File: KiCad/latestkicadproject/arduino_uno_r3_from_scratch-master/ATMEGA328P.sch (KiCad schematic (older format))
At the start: 12 parts, among them SW1 RESET_SWITCH, U5 ATMEGA328P, X2 CSTCE16MOV53-R0

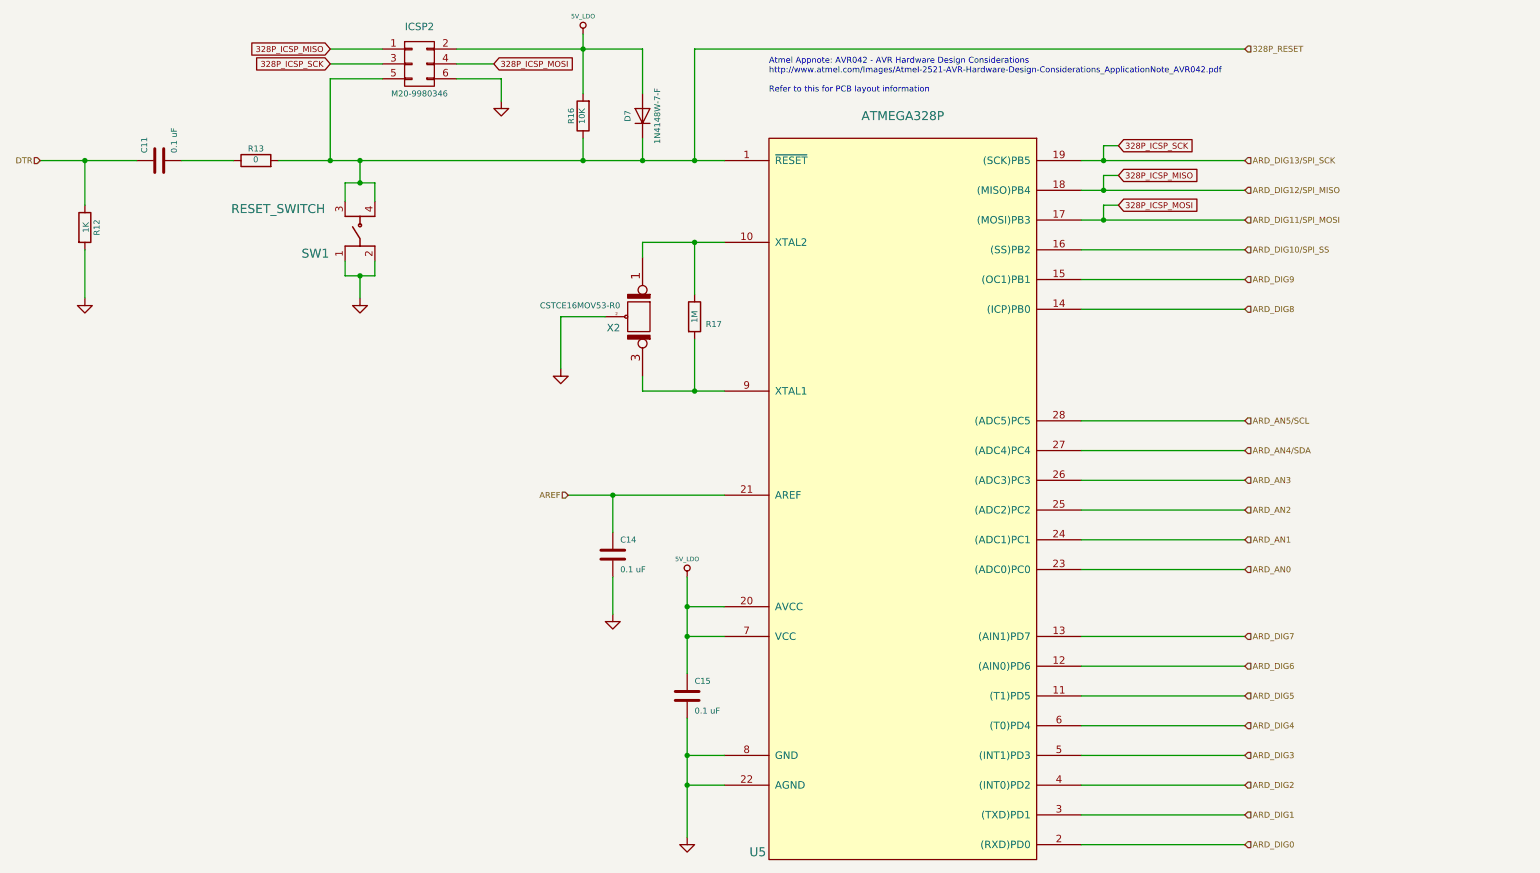
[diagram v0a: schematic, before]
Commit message: 28feb
Aanpassing KiCad+deel footprints
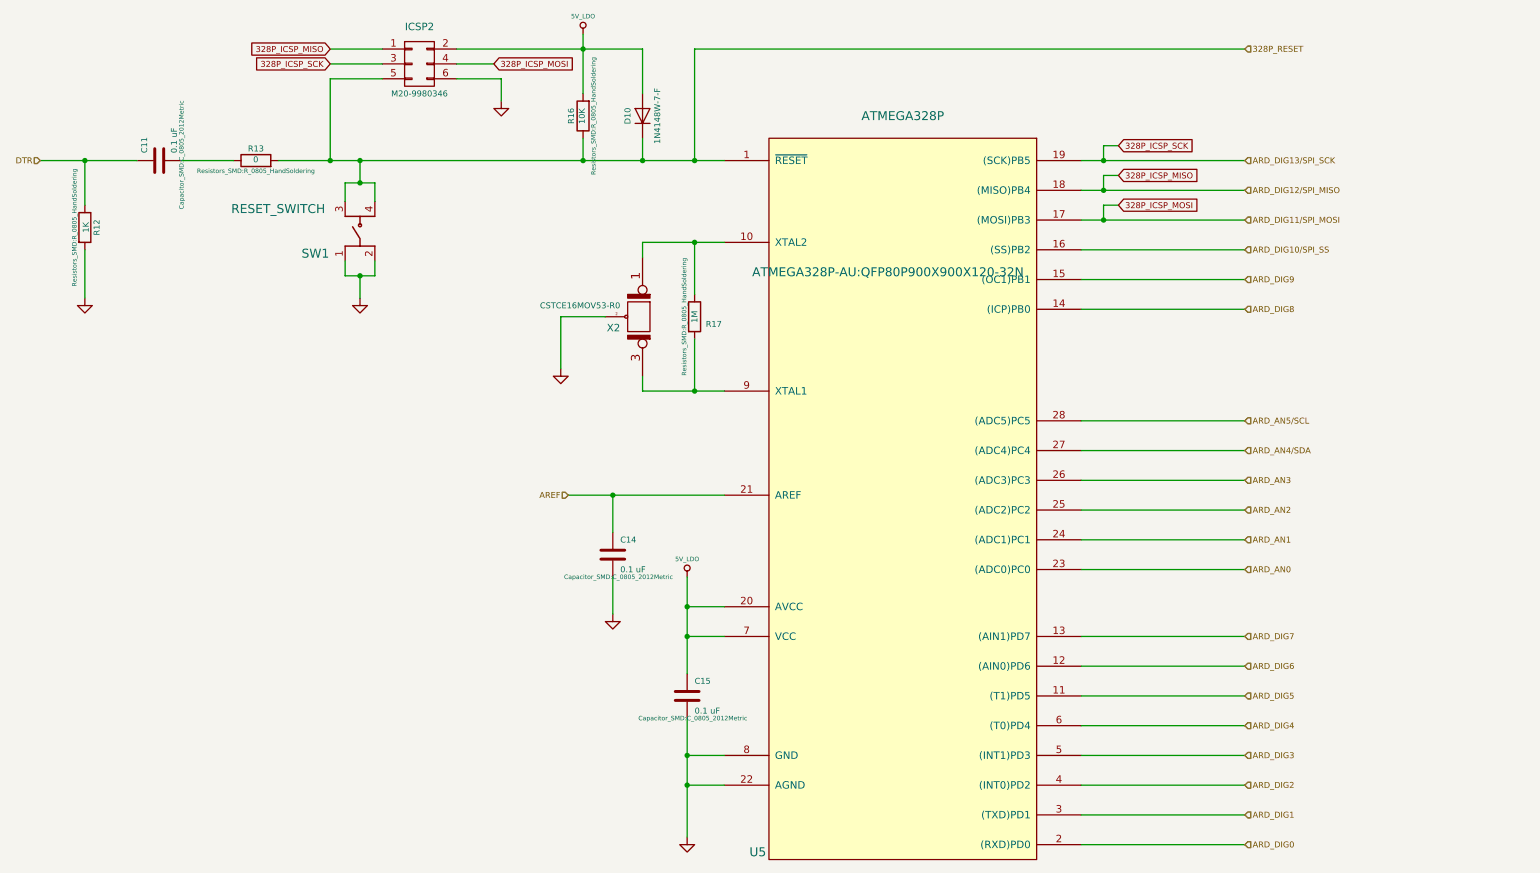
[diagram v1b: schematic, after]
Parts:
- C11, C14, C15: footprint ~ -> Capacitor_SMD:C_0805_2012Metric
- D10: renamed from D7; footprint ~ -> (none)
- ICSP2, X2: footprint ~ -> (none)
- R12, R13, R16, R17: footprint ~ -> Resistors_SMD:R_0805_HandSoldering
- U5: footprint ~ -> ATMEGA328P-AU:QFP80P900X900X120-32N
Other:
- note removed: "Atmel Appnote: AVR042 - AVR Hardware Design Considerations\nhttp://www.atmel.com/Images/Atmel-2521-AVR-Hardware-Design-Considerations_ApplicationNote_AVR042.pdf\n\nRefer to this for PCB layout information"
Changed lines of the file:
@@
 $Descr A4 11693 8268
 encoding utf-8
-Sheet 5 7
+Sheet 7 7
 Title "Arduino UNO R3 Clone"
 Date "8 oct 2015"
@@
 F 0 "U5" H 6075 1350 60  0000 C CNN
 F 1 "ATMEGA328P" H 7050 6300 60  0000 C CNN
-F 2 "~" H 6950 5250 60  0000 C CNN
+F 2 "ATMEGA328P-AU:QFP80P900X900X120-32N" H 6950 5250 60  0000 C CNN
 F 3 "http://www.atmel.com/images/Atmel-8271-8-bit-AVR-Microcontroller-ATmega48A-48PA-88A-88PA-168A-168PA-328-328P_datasheet_Complete.pdf" H 6950 5250 60  0001 C CNN
 F 4 "IC MCU 8BIT 32KB FLASH 28DIP" H 7050 3750 60  0001 C CNN "Characteristics"
@@
 	4800 3750 5850 3750
 $Comp
-L GND-RESCUE-Arduino_Uno_R3_From_Scratch #PWR020
+L GND-RESCUE-Arduino_Uno_R3_From_Scratch #PWR033
 U 1 1 55E8AA8C
 P 5600 6050
-F 0 "#PWR020" H 5600 6050 30  0001 C CNN
+F 0 "#PWR033" H 5600 6050 30  0001 C CNN
 F 1 "GND" H 5600 5980 30  0001 C CNN
 F 2 "~" H 5600 6050 60  0000 C CNN
@@
 F 0 "R12" V 1630 1950 40  0000 C CNN
 F 1 "1K" V 1557 1951 40  0000 C CNN
-F 2 "~" V 1480 1950 30  0000 C CNN
+F 2 "Resistors_SMD:R_0805_HandSoldering" V 1480 1950 30  0000 C CNN
 F 3 "http://images.ihscontent.net/vipimages/VipMasterIC/IC/VISH/VISHS75859/VISHS75859-1.pdf" H 1550 1950 30  0001 C CNN
 F 4 "METAL GLAZE/THICK FILM, 0.125W, 5%, 200ppm, 1000ohm, SURFACE MOUNT, 0805," H 1550 1950 60  0001 C CNN "Characteristics"
@@
 F 0 "ICSP2" H 3800 1100 50  0000 C CNN
 F 1 "M20-9980346" H 3800 650 40  0000 C CNN
-F 2 "~" H 3800 850 60  0000 C CNN
+F 2 "" H 3800 850 60  0000 C CNN
 F 3 "http://cdn.harwin.com/pdfs/M20-998.pdf" H 3800 850 60  0001 C CNN
 F 4 "6 CONTACT(S), MALE, STRAIGHT TWO PART BOARD CONNECTOR" H 3800 850 60  0001 C CNN "Characteristics"
@@
 $EndComp
 $Comp
-L D D7
+L D D10
 U 1 1 55E8CABC
 P 5300 1200
-F 0 "D7" H 5300 1300 40  0000 C CNN
+F 0 "D10" H 5300 1300 40  0000 C CNN
 F 1 "1N4148W-7-F" H 5300 1100 40  0000 C CNN
-F 2 "~" H 5300 1200 60  0000 C CNN
+F 2 "" H 5300 1200 60  0000 C CNN
 F 3 "http://www.diodes.com/_files/datasheets/ds30086.pdf" H 5300 1200 60  0001 C CNN
 F 4 "DIODE GEN PURP 100V 300MA SOD123" H 5300 1200 60  0001 C CNN "Characteristics"
@@
 F 0 "SW1" V 3250 2275 60  0000 C CNN
 F 1 "RESET_SWITCH" V 3550 2525 60  0000 C CNN
-F 2 "" H 3400 1975 60  0000 C CNN
+F 2 "" H 3400 1975 60  0001 C CNN
 F 3 "http://industrial.panasonic.com/www-data/pdf/ATK0000/ATK0000CE28.pdf" H 3400 1975 60  0001 C CNN
 F 4 "SWITCH TACTILE SPST-NO 0.02A 15V" H 3400 1975 60  0001 C CNN "Characteristics"
@@
 	3200 950  3200 1500
 $Comp
-L 5V_LDO #PWR021
+L 5V_LDO #PWR034
 U 1 1 55E95BB4
 P 4900 650
-F 0 "#PWR021" H 4900 740 20  0001 C CNN
+F 0 "#PWR034" H 4900 740 20  0001 C CNN
 F 1 "5V_LDO" H 4900 770 30  0000 C CNN
 F 2 "~" H 4900 650 60  0000 C CNN
@@
 $EndComp
 $Comp
-L 5V_LDO #PWR022
+L 5V_LDO #PWR035
 U 1 1 55E95BC3
 P 5600 4300
-F 0 "#PWR022" H 5600 4390 20  0001 C CNN
+F 0 "#PWR035" H 5600 4390 20  0001 C CNN
 F 1 "5V_LDO" H 5600 4420 30  0000 C CNN
 F 2 "~" H 5600 4300 60  0000 C CNN
@@
 F 0 "R13" V 2780 1500 40  0000 C CNN
 F 1 "0" V 2707 1501 40  0000 C CNN
-F 2 "~" V 2630 1500 30  0000 C CNN
+F 2 "Resistors_SMD:R_0805_HandSoldering" V 2630 1500 30  0000 C CNN
 F 3 "http://industrial.panasonic.com/www-cgi/jvcr13pz.cgi?E+PZ+3+AOA0001+ERJ6GEY0R00V+7+WW" H 2700 1500 30  0001 C CNN
 F 4 "RES SMD 0.0 OHM JUMPER 1/8W 0805" H 2700 1500 60  0001 C CNN "Characteristics"
@@
 F 0 "X2" V 5325 2450 50  0000 R CNN
 F 1 "CSTCE16MOV53-R0" V 5175 2450 40  0000 R CNN
-F 2 "~" H 5250 2550 60  0000 C CNN
+F 2 "" H 5250 2550 60  0000 C CNN
 F 3 "http://www.murata.com/~/media/webrenewal/support/library/catalog/products/timingdevice/ceralock/p16e.ashx" H 5250 2550 60  0001 C CNN
 F 4 "CER RESONATOR 16.0MHZ SMD" H 5250 2550 60  0001 C CNN "Characteristics"
@@
 Wire Wire Line
 	4750 2550 4750 2900
-Text Notes 6150 1050 0    40   ~ 0
-Atmel Appnote: AVR042 - AVR Hardware Design Considerations\nhttp://www.atmel.com/Images/Atmel-2521-AVR-Hardware-Design-Considerations_ApplicationNote_AVR042.pdf\n\nRefer to this for PCB layout information
 $Comp
 L C C14
@@
 F 0 "C14" H 5150 4250 40  0000 L CNN
 F 1 "0.1 uF" H 5150 4050 40  0000 L CNN
-F 2 "~" H 5138 4000 30  0000 C CNN
+F 2 "Capacitor_SMD:C_0805_2012Metric" H 5138 4000 30  0000 C CNN
 F 3 "http://images.ihscontent.net/vipimages/VipMasterIC/IC/KEME/KEMES10043/KEMES10043-1.pdf" H 5100 4150 60  0001 C CNN
 F 4 "CAPACITOR, CERAMIC, MULTILAYER, 100 V, X7R, 0.1 uF, SURFACE MOUNT, 0805, CHIP, ROHS COMPLIANT" H 5100 4150 60  0001 C CNN "Characteristics"
@@
 F 0 "C15" H 5650 5200 40  0000 L CNN
 F 1 "0.1 uF" H 5650 5000 40  0000 L CNN
-F 2 "~" H 5638 4950 30  0000 C CNN
+F 2 "Capacitor_SMD:C_0805_2012Metric" H 5638 4950 30  0000 C CNN
 F 3 "http://images.ihscontent.net/vipimages/VipMasterIC/IC/KEME/KEMES10043/KEMES10043-1.pdf" H 5600 5100 60  0001 C CNN
 F 4 "CAPACITOR, CERAMIC, MULTILAYER, 100 V, X7R, 0.1 uF, SURFACE MOUNT, 0805, CHIP, ROHS COMPLIANT" H 5600 5100 60  0001 C CNN "Characteristics"
@@
 F 0 "R16" V 4980 1200 40  0000 C CNN
 F 1 "10K" V 4907 1201 40  0000 C CNN
-F 2 "~" V 4830 1200 30  0000 C CNN
+F 2 "Resistors_SMD:R_0805_HandSoldering" V 4830 1200 30  0000 C CNN
 F 3 "http://images.ihscontent.net/vipimages/VipMasterIC/IC/VISH/VISHS75859/VISHS75859-1.pdf" H 4900 1200 30  0001 C CNN
 F 4 "RESISTOR, METAL GLAZE/THICK FILM, 0.125W, 5%, 200ppm, 10000ohm, SURFACE MOUNT, 0805" H 4900 1200 60  0001 C CNN "Characteristics"
@@
 F 0 "C11" H 2100 1600 40  0000 L CNN
 F 1 "0.1 uF" H 2100 1400 40  0000 L CNN
-F 2 "~" H 2088 1350 30  0000 C CNN
+F 2 "Capacitor_SMD:C_0805_2012Metric" H 2088 1350 30  0000 C CNN
 F 3 "http://images.ihscontent.net/vipimages/VipMasterIC/IC/KEME/KEMES10043/KEMES10043-1.pdf" H 2050 1500 60  0001 C CNN
 F 4 "CAPACITOR, CERAMIC, MULTILAYER, 100 V, X7R, 0.1 uF, SURFACE MOUNT, 0805, CHIP, ROHS COMPLIANT" H 2050 1500 60  0001 C CNN "Characteristics"
@@
 F 0 "R17" H 5725 2500 40  0000 L CNN
 F 1 "1M" V 5650 2550 40  0000 C CNN
-F 2 "~" V 5580 2550 30  0000 C CNN
+F 2 "Resistors_SMD:R_0805_HandSoldering" V 5580 2550 30  0000 C CNN
 F 3 "http://www.vishay.com/docs/20035/dcrcwe3.pdf" H 5650 2550 30  0001 C CNN
 F 4 "RES SMD 1M OHM 1% 1/8W 0805" H 5650 2550 60  0001 C CNN "Characteristics"
@@
 	3300 2275 3300 2175
 $Comp
-L GND-RESCUE-Arduino_Uno_R3_From_Scratch #PWR023
+L GND-RESCUE-Arduino_Uno_R3_From_Scratch #PWR036
 U 1 1 562077A6
 P 5100 4550
-F 0 "#PWR023" H 5100 4550 30  0001 C CNN
+F 0 "#PWR036" H 5100 4550 30  0001 C CNN
 F 1 "GND" H 5100 4480 30  0001 C CNN
 F 2 "~" H 5100 4550 60  0000 C CNN
@@
 $EndComp
 $Comp
-L GND-RESCUE-Arduino_Uno_R3_From_Scratch #PWR024
+L GND-RESCUE-Arduino_Uno_R3_From_Scratch #PWR037
 U 1 1 56207870
 P 4750 2900
-F 0 "#PWR024" H 4750 2900 30  0001 C CNN
+F 0 "#PWR037" H 4750 2900 30  0001 C CNN
 F 1 "GND" H 4750 2830 30  0001 C CNN
 F 2 "~" H 4750 2900 60  0000 C CNN
@@
 $EndComp
 $Comp
-L GND-RESCUE-Arduino_Uno_R3_From_Scratch #PWR025
+L GND-RESCUE-Arduino_Uno_R3_From_Scratch #PWR038
 U 1 1 562079B8
 P 3400 2425
-F 0 "#PWR025" H 3400 2425 30  0001 C CNN
+F 0 "#PWR038" H 3400 2425 30  0001 C CNN
 F 1 "GND" H 3400 2355 30  0001 C CNN
 F 2 "~" H 3400 2425 60  0000 C CNN
@@
 $EndComp
 $Comp
-L GND-RESCUE-Arduino_Uno_R3_From_Scratch #PWR026
+L GND-RESCUE-Arduino_Uno_R3_From_Scratch #PWR039
 U 1 1 56207AE4
 P 1550 2425
-F 0 "#PWR026" H 1550 2425 30  0001 C CNN
+F 0 "#PWR039" H 1550 2425 30  0001 C CNN
 F 1 "GND" H 1550 2355 30  0001 C CNN
 F 2 "~" H 1550 2425 60  0000 C CNN
@@
 $EndComp
 $Comp
-L GND-RESCUE-Arduino_Uno_R3_From_Scratch #PWR027
+L GND-RESCUE-Arduino_Uno_R3_From_Scratch #PWR040
 U 1 1 56208C49
 P 4350 1100
-F 0 "#PWR027" H 4350 1100 30  0001 C CNN
+F 0 "#PWR040" H 4350 1100 30  0001 C CNN
 F 1 "GND" H 4350 1030 30  0001 C CNN
 F 2 "~" H 4350 1100 60  0000 C CNN

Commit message: Toevoegen footprints Kicad
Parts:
- D10: footprint (none) -> 1N4148W-7-F:SOD3716X115N
- X2: footprint (none) -> CSTCE16M0V53-R0:OSC_CSTCE16M0V53-R0
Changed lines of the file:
@@
 F 0 "ICSP2" H 3800 1100 50  0000 C CNN
 F 1 "M20-9980346" H 3800 650 40  0000 C CNN
-F 2 "" H 3800 850 60  0000 C CNN
+F 2 "" H 3800 850 60  0001 C CNN
 F 3 "http://cdn.harwin.com/pdfs/M20-998.pdf" H 3800 850 60  0001 C CNN
 F 4 "6 CONTACT(S), MALE, STRAIGHT TWO PART BOARD CONNECTOR" H 3800 850 60  0001 C CNN "Characteristics"
@@
 F 0 "D10" H 5300 1300 40  0000 C CNN
 F 1 "1N4148W-7-F" H 5300 1100 40  0000 C CNN
-F 2 "" H 5300 1200 60  0000 C CNN
+F 2 "1N4148W-7-F:SOD3716X115N" H 5300 1200 60  0001 C CNN
 F 3 "http://www.diodes.com/_files/datasheets/ds30086.pdf" H 5300 1200 60  0001 C CNN
 F 4 "DIODE GEN PURP 100V 300MA SOD123" H 5300 1200 60  0001 C CNN "Characteristics"
@@
 	0    -1   -1   0
 $EndComp
-$Comp
-L CERAMIC_RESONATOR X2
-U 1 1 5614A1DB
-P 5250 2550
-F 0 "X2" V 5325 2450 50  0000 R CNN
-F 1 "CSTCE16MOV53-R0" V 5175 2450 40  0000 R CNN
-F 2 "" H 5250 2550 60  0000 C CNN
-F 3 "http://www.murata.com/~/media/webrenewal/support/library/catalog/products/timingdevice/ceralock/p16e.ashx" H 5250 2550 60  0001 C CNN
-F 4 "CER RESONATOR 16.0MHZ SMD" H 5250 2550 60  0001 C CNN "Characteristics"
-F 5 "ATMEGA328P Oscillator" H 5250 2550 60  0001 C CNN "Description"
-F 6 "Murata" H 5250 2550 60  0001 C CNN "MFN"
-F 7 "CSTCE16M0V53-R0" H 5250 2550 60  0001 C CNN "MFP"
-F 8 "SMD" H 5250 2550 60  0001 C CNN "Package ID"
-F 9 "ANY" H 5250 2550 60  0001 C CNN "Source"
-F 10 "Y" H 5250 2550 60  0001 C CNN "Critical"
-F 11 "328P_Sub" H 5250 2550 60  0001 C CNN "Subsystem"
-F 12 "~" H 5250 2550 60  0001 C CNN "Notes"
-	1    5250 2550
-	0    1    1    0
-$EndComp
 Wire Wire Line
 	5300 2050 5850 2050
@@
 Wire Wire Line
 	5300 3050 5850 3050
-Wire Wire Line
-	5050 2550 4750 2550
 Wire Wire Line
 	4750 2550 4750 2900
@@
 	1    0    0    -1
 $EndComp
+$Comp
+L CERAMIC_RESONATOR X2
+U 1 1 5614A1DB
+P 5250 2550
+F 0 "X2" V 5325 2450 50  0000 R CNN
+F 1 "CSTCE16MOV53-R0" V 5175 2450 40  0000 R CNN
+F 2 "CSTCE16M0V53-R0:OSC_CSTCE16M0V53-R0" H 5250 2550 60  0001 C CNN
+F 3 "http://www.murata.com/~/media/webrenewal/support/library/catalog/products/timingdevice/ceralock/p16e.ashx" H 5250 2550 60  0001 C CNN
+F 4 "CER RESONATOR 16.0MHZ SMD" H 5250 2550 60  0001 C CNN "Characteristics"
+F 5 "ATMEGA328P Oscillator" H 5250 2550 60  0001 C CNN "Description"
+F 6 "Murata" H 5250 2550 60  0001 C CNN "MFN"
+F 7 "CSTCE16M0V53-R0" H 5250 2550 60  0001 C CNN "MFP"
+F 8 "SMD" H 5250 2550 60  0001 C CNN "Package ID"
+F 9 "ANY" H 5250 2550 60  0001 C CNN "Source"
+F 10 "Y" H 5250 2550 60  0001 C CNN "Critical"
+F 11 "328P_Sub" H 5250 2550 60  0001 C CNN "Subsystem"
+F 12 "~" H 5250 2550 60  0001 C CNN "Notes"
+	1    5250 2550
+	0    1    1    0
+$EndComp
+Wire Wire Line
+	5050 2550 4750 2550
 $EndSCHEMATC
